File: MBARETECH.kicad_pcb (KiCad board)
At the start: 2 copper layers, 100 x 100 mm, 53 parts, among them SW1 SW1, SW2 SW2, U1 ESP32-S3-DEVKITC-1-N8R2

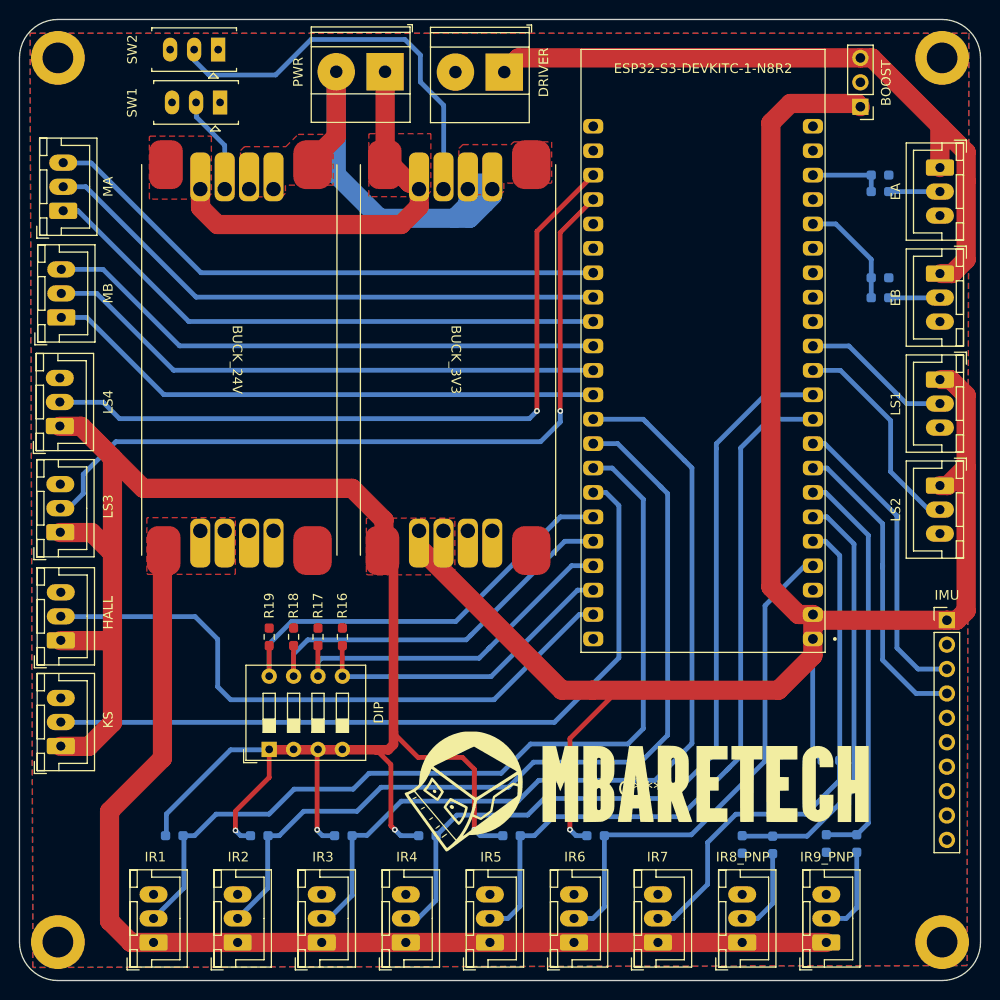
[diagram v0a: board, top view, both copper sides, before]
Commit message: Connect -BATT2GND
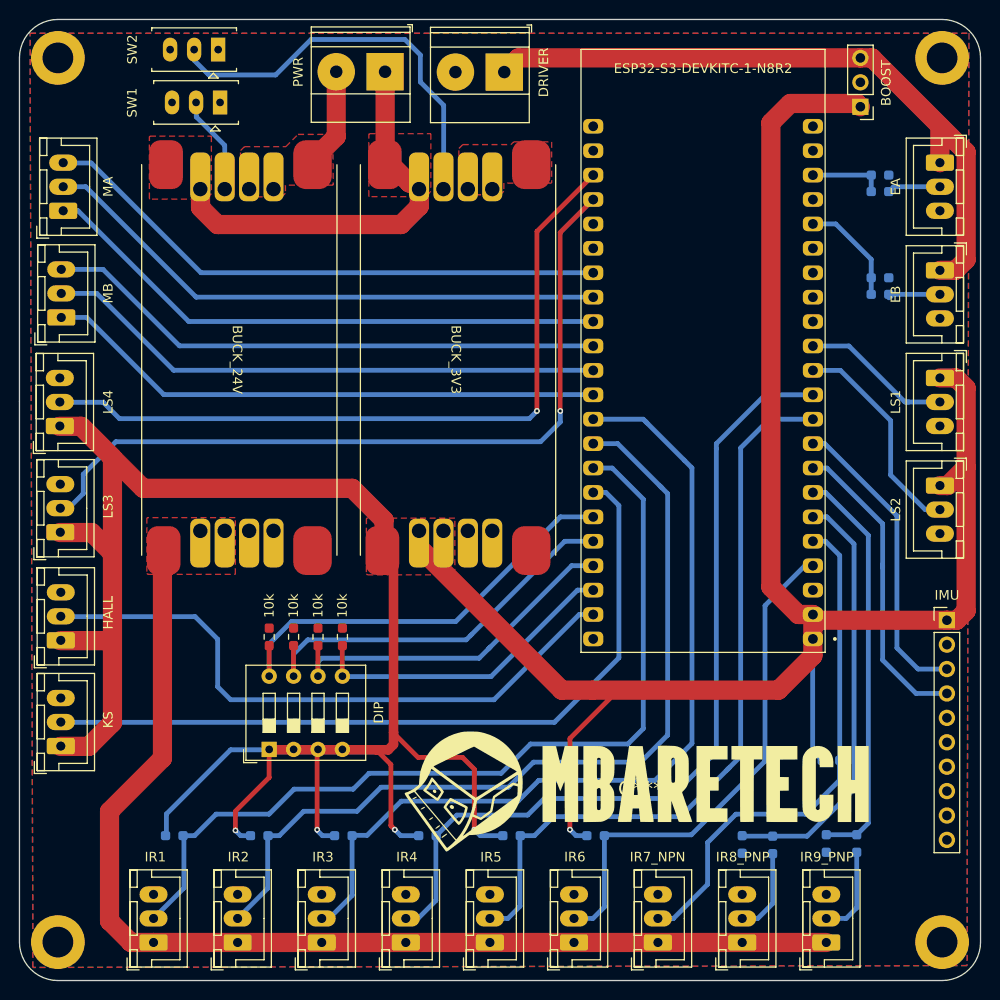
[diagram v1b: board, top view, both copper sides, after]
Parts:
- IR7: value IR7 -> IR7_NPN
- R16: value R16 -> 10k
- R17: value R17 -> 10k
- R18: value R18 -> 10k
- R19: value R19 -> 10k
- moved EA1 0.51 mm to (192.8, 67.6)
- moved R14 0.35 mm to (186.5, 81.3)
- moved EB1 0.34 mm to (192.8, 78.8)
- moved LS1 0.17 mm to (192.8, 90.0)
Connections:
- BUCK1 pad 5: GND -> -BATT
- BUCK2 pad 5: GND -> -BATT
- Boost1 pad 2: GND -> -BATT
- DRIVER1 pad 2: GND -> -BATT
- EA1 pad 3: GND -> -BATT
- EB1 pad 3: GND -> -BATT
- HALL1 pad 3: GND -> -BATT
- IMU1 pad 2: GND -> -BATT
- IR1 pad 3: GND -> -BATT
- IR2 pad 3: GND -> -BATT
- IR3 pad 3: GND -> -BATT
- IR4 pad 3: GND -> -BATT
- IR5 pad 3: GND -> -BATT
- IR6_NPN1 pad 3: GND -> -BATT
- IR7 pad 3: GND -> -BATT
- IR8 pad 3: GND -> -BATT
- IR9 pad 3: GND -> -BATT
- KS1 pad 3: GND -> -BATT
- LS1 pad 3: GND -> -BATT
- LS2 pad 3: GND -> -BATT
- LS3 pad 3: GND -> -BATT
- LS4 pad 3: GND -> -BATT
- R11 pad 2: GND -> -BATT
- R13 pad 2: GND -> -BATT
- R15 pad 2: GND -> -BATT
- R16 pad 2: GND -> -BATT
- R17 pad 2: GND -> -BATT
- R18 pad 2: GND -> -BATT
- R19 pad 2: GND -> -BATT
- R9 pad 2: GND -> -BATT
- SW1 pad 3: GND -> -BATT
- SW2 pad 3: GND -> -BATT
- U1 pad J1_22: GND -> -BATT
- U1 pad J3_1: GND -> -BATT
- U1 pad J3_21: GND -> -BATT
- U1 pad J3_22: GND -> -BATT
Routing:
- net -BATT: track 50.9 -> 10.2 mm
- net +3V3: track 390.5 -> 391.0 mm
- net +5V: track 71.5 -> 71.0 mm
- added copper zone on B.Cu, net -BATT
- removed copper zone on B.Cu, net GND
- removed copper zone on F.Cu, net GND
